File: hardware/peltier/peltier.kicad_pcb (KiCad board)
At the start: 2 copper layers, 71 x 45.5 mm, 39 parts, among them J1 Conn_01x02, J2 Conn_01x04, J3 Conn_01x04, J5 Conn_01x02, J6 Conn_01x03, Q1 IRF5305PbF, Q2 IRF5305PbF, Q3 IRFZ44NPbF, Q4 IRFZ44NPbF, U1 TC4420CPA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

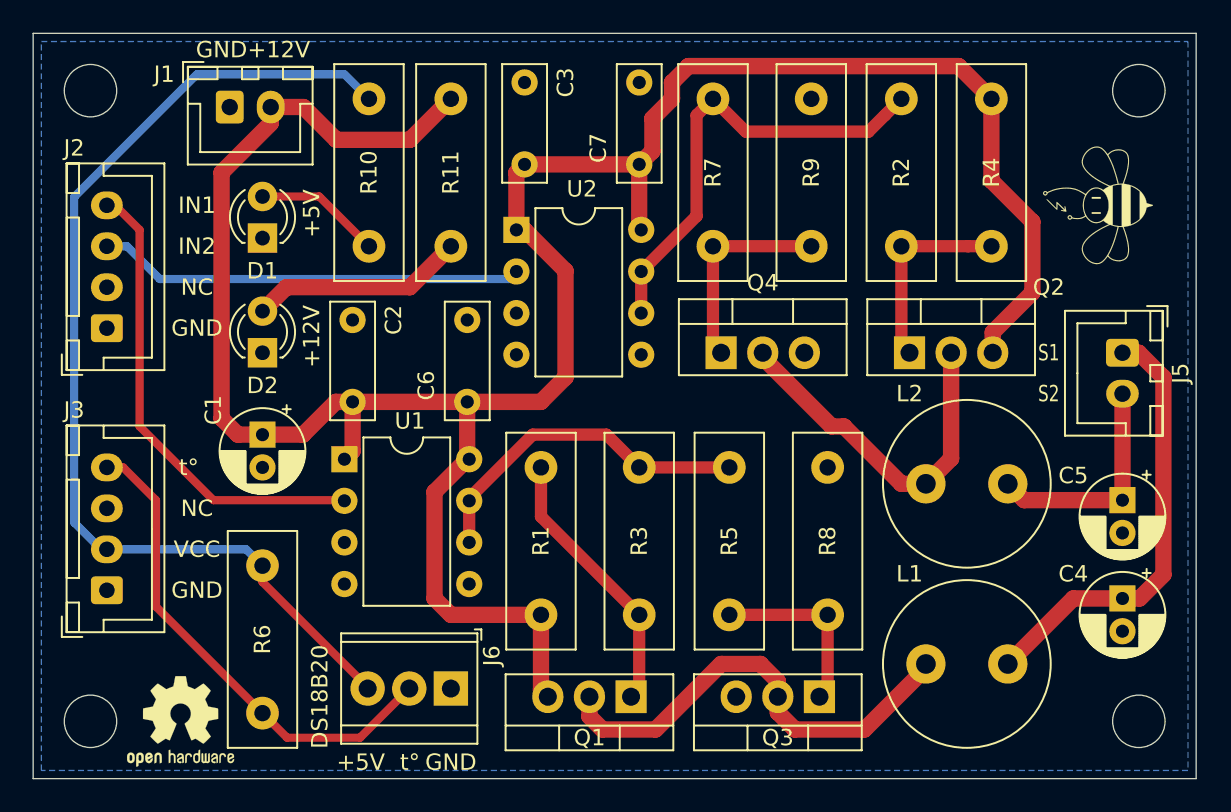
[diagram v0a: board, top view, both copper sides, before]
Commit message: Quick pinout fix for Peltier driver
Simple fix with  pinout now being correct
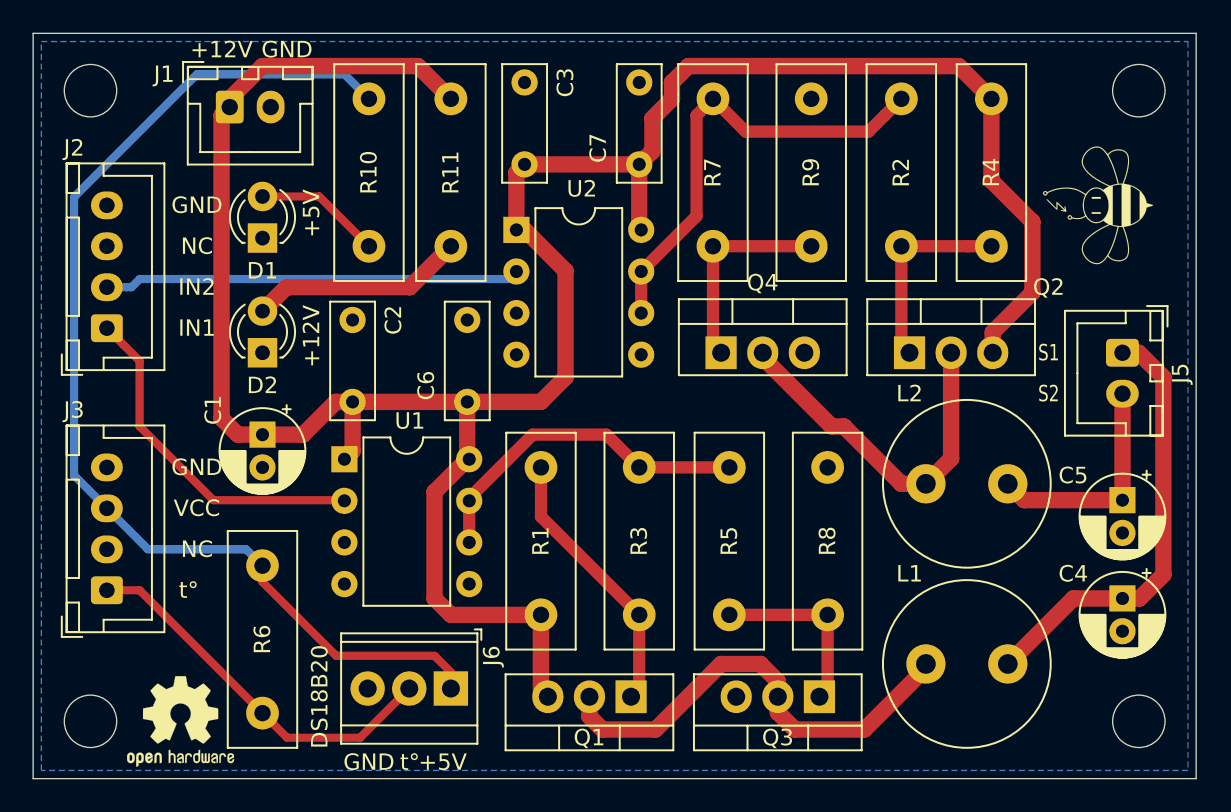
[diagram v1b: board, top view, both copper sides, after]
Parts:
- Q1, Q2: value IRF5305PbF -> IRF9Z34NPBF
- Q3, Q4: value IRFZ44NPbF -> IRFZ24NPBF
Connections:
- J1 pad 1: GND -> +12V
- J1 pad 2: +12V -> GND
- J2 pad 1: GND -> IN1
- J2 pad 2: Net-(J2-Pad2) -> IN2
- J2 pad 3: IN2 -> Net-(J2-Pad3)
- J2 pad 4: IN1 -> GND
- J3 pad 1: GND -> t
- J3 pad 2: +5V -> Net-(J3-Pad2)
- J3 pad 3: Net-(J3-Pad3) -> +5V
- J3 pad 4: t -> GND
- J6 pad 1: GND -> +5V
- J6 pad 3: +5V -> GND
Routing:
- net IN1: track 29.0 -> 21.2 mm
- net t: track 30.3 -> 23.4 mm
- net +5V: track 64.3 -> 68.3 mm
- net +12V: track 154.7 -> 156.4 mm
- net IN2: track 26.0 -> 25.4 mm
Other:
- rule pad_to_mask_clearance: 0.051 -> 0

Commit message: Update on 12V5A system power line
- 12V5A power line is now represented by two connectors with 2 pins across all the modules
- all .png previews are updated. The central hub now has previews for schematics, PCB tracing and 3D model
- peltier module now has two 12V5A connectors with redesigned one side of the bridge. Now all MOSFETs can be equipped with heatsinks
- hum/temp sensor now has its connector position reversed to mimic Grove's one
- hum/temp and gas sensors now have a small BeeHive logo on front layer rather than one big on back layer
- hum/temp sensor now use only one layer for signals and one layer for ground
- switch arrays now have two connectors for 12V5A and 5V3A power lines
- switch arrays had their power lines better traced (no sharp turns)
- power supply (12V5A to 5V3A) now has two connectors for 12V5A power line
- one trace of power supply, which lies in between LM2596's legs, was narrowed to ensure that it will not be accidentally soldered or damaged during placement
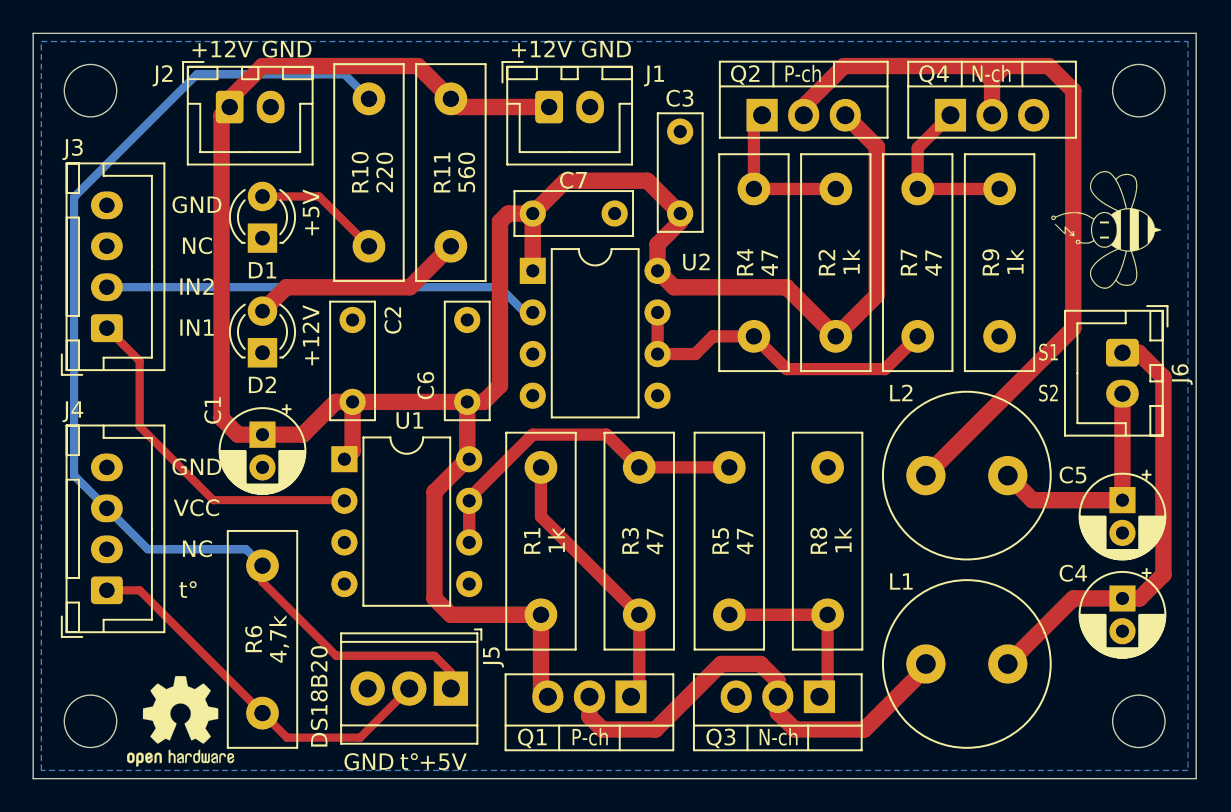
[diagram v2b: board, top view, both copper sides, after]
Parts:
- added J1: Conn_01x02, Connector_JST:JST_XH_B2B-XH-A_1x02_P2.50mm_Vertical, F.Cu at (155.5, 75.5)
- moved Q4 20.2 mm to (180.0, 76.0)
- moved R7 19.1 mm to (178.0, 89.5), turned to 90 degrees
- moved R9 18.5 mm to (183.0, 89.5), turned to 90 degrees
- moved Q2 17.1 mm to (168.5, 76.0)
- moved R4 17.1 mm to (168.0, 89.5), turned to 90 degrees
- moved R2 10.1 mm to (173.0, 80.5), turned to 270 degrees
- moved C3 9.96 mm to (163.5, 82.0)
- moved C7 7.16 mm to (154.5, 82.0), turned to 0 degrees
- moved U2 2.69 mm to (154.5, 85.5)
- moved G*** 1.58 mm to (189.5, 83.0)
- moved L2 0.50 mm to (178.5, 98.0)
- renumbered J1 to J2, J2 to J3, J3 to J4, J6 to J5, J5 to J6
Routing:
- net Net-(L2-Pad1): track 22.1 -> 50.8 mm
- net +12V: track 156.4 -> 146.8 mm
- net Net-(R4-Pad1): track 28.1 -> 20.5 mm
- net Net-(Q2-Pad1): track 12.2 -> 9.71 mm
- net Net-(Q4-Pad1): track 12.7 -> 10.3 mm
- net IN2: track 25.4 -> 26.6 mm
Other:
- board text added: "1k"
- board text added: "220"
- board text added: "4,7k"
- board text added: "47"
- board text added: "560"
- board text added: "N-ch"
- board text added: "P-ch"

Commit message: Add version number to boards
Add version number to boards and update screenshots, zip gerber archives
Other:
- board text added: "Peltier board v0.1"
